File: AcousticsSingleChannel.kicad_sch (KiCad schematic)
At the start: 24 parts, among them J1 SSW-104-01-G-D, J2 TSW-104-07-F-D, U1 OPA1604AIPWR, U2 ADS127L21IRUKT, U4 mcp1416t-e/ot

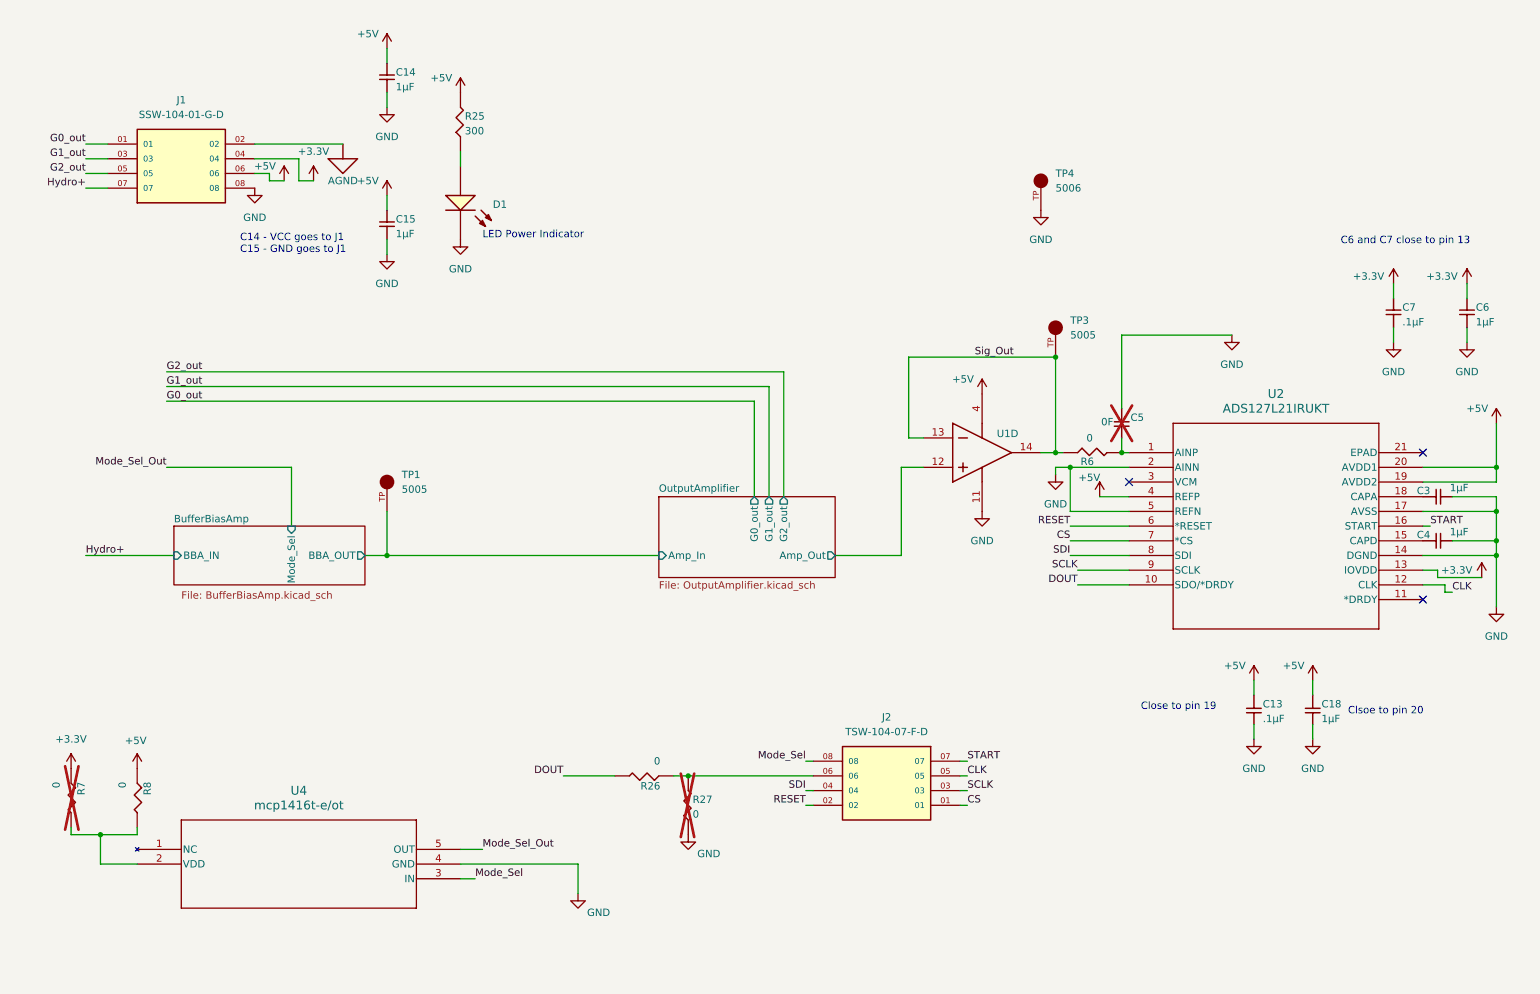
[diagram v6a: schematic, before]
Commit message: Changed headers.
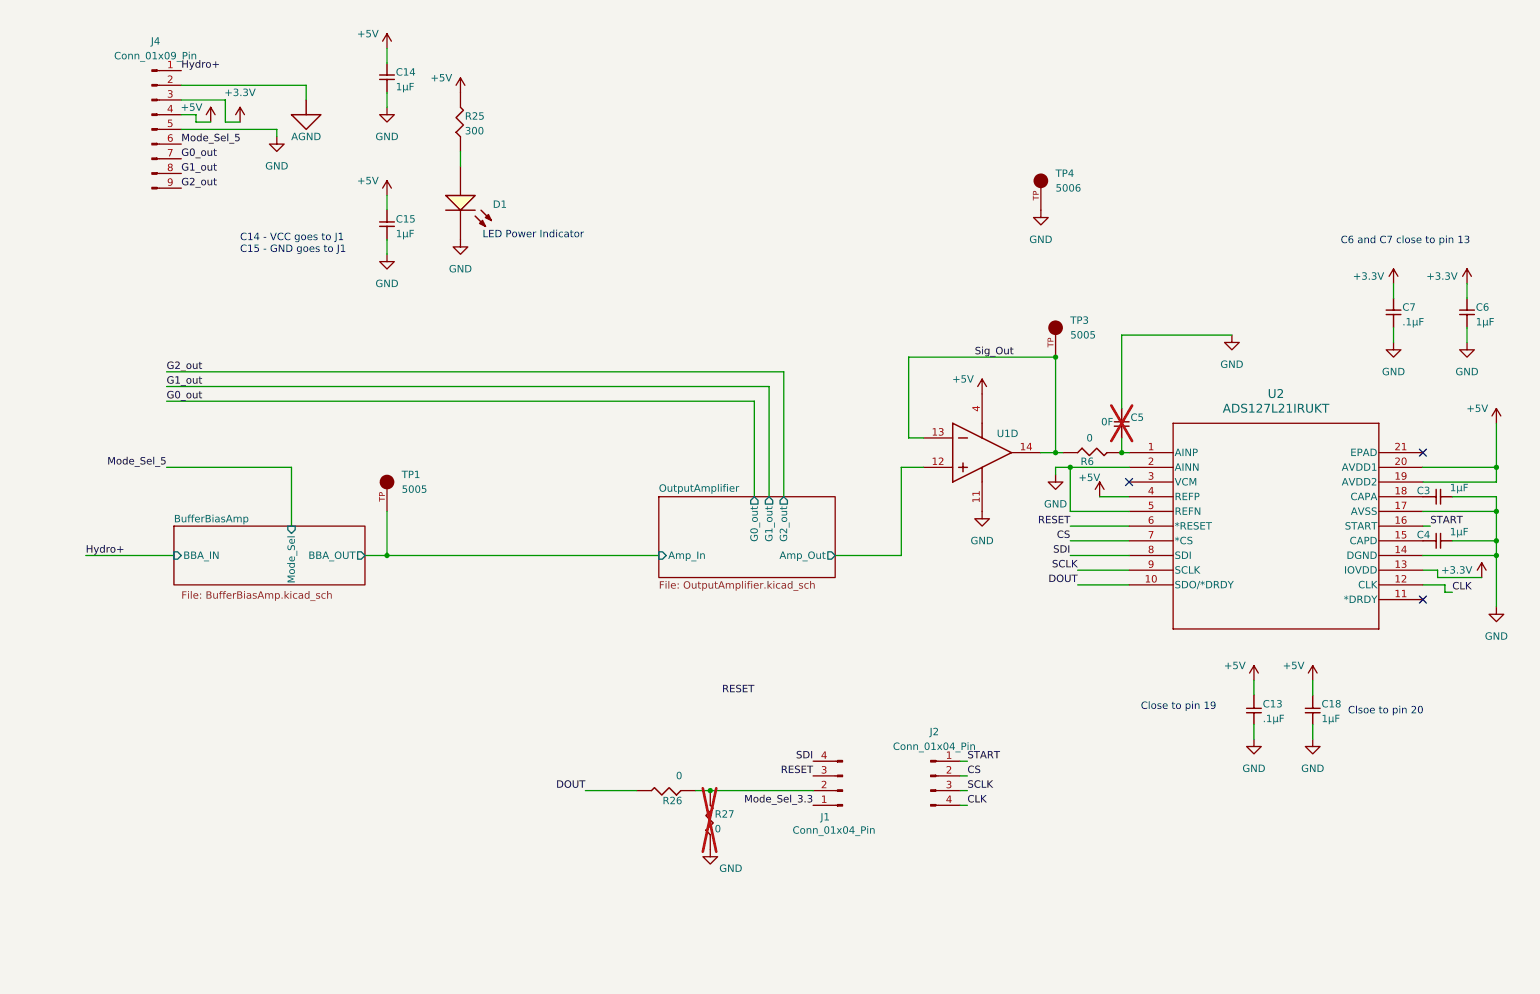
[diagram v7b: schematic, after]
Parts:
- removed J1: SSW-104-01-G-D, Accoustics:SAMTEC_SSW-104-01-G-D, symbol Accoustics:SSW-104-01-G-D
- removed J2: TSW-104-07-F-D, Accoustics:SAMTEC_TSW-104-07-F-D, symbol Accoustics:TSW-104-07-F-D
- removed R7, R8: 0, AltiumImports:SMD-0603-RES, symbol AcousticsSingleChannel-altium-import:root_0_ERJ-3EKF7500V
- removed U4: mcp1416t-e/ot, Accoustics:SOT-23-5_MC_MCH-M, symbol Accoustics:mcp1416t-e_ot
- added J1, J2: Conn_01x04_Pin, Connector_PinHeader_2.54mm:PinHeader_1x04_P2.54mm_Vertical, symbol Connector:Conn_01x04_Pin
- added J4: Conn_01x09_Pin, Connector_PinHeader_2.54mm:PinHeader_1x09_P2.54mm_Vertical, symbol Connector:Conn_01x09_Pin
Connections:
- net +3.3V: now also J4.3 (Pin_3)
- net +5V: now also J4.4 (Pin_4)
- net AGND: now also J4.2 (Pin_2)
- net CLK: now also J2.4 (Pin_4)
- net CS: now also J2.2 (Pin_2)
- net G0_out: now also J4.7 (Pin_7)
- net G1_out: now also J4.8 (Pin_8)
- net G2_out: now also J4.9 (Pin_9)
- net GND: now also J4.5 (Pin_5)
- net Hydro+: now also J4.1 (Pin_1)
- net RESET: now also J1.3 (Pin_3)
- net SCLK: now also J2.3 (Pin_3)
- net SDI: now also J1.4 (Pin_4)
- net START: now also J2.1 (Pin_1)
- net at R26.1, R27.2: now also J1.2 (Pin_2)
- new net Mode_Sel_3.3: J1.1 (Pin_1)
- new net Mode_Sel_5: J4.6 (Pin_6)
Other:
- moved on the sheet: R26, R27

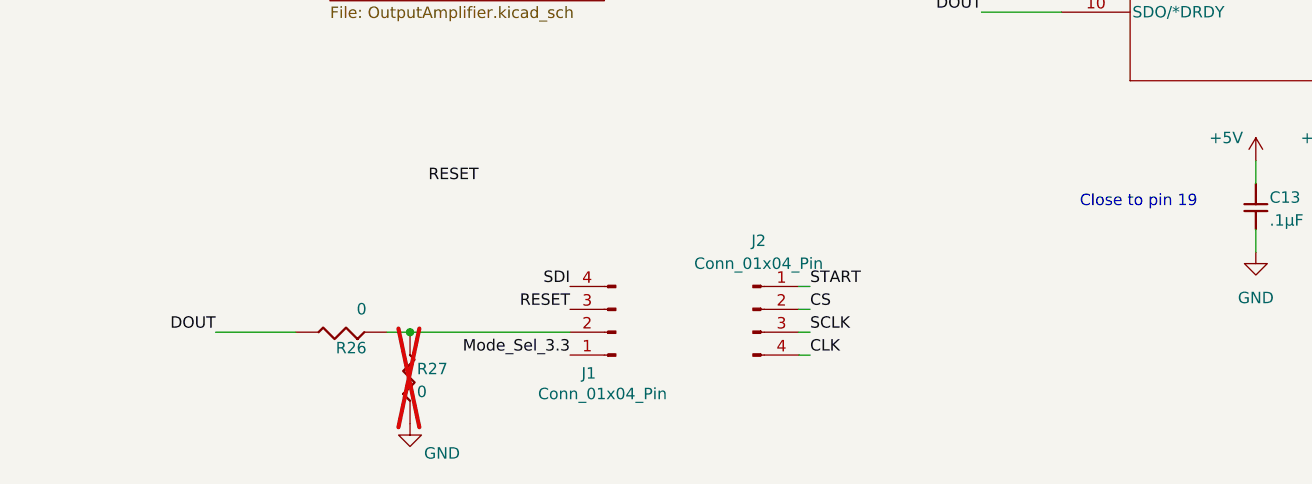
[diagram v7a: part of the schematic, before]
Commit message: changed pinouts, causing major changes to layout mostly on layer1.
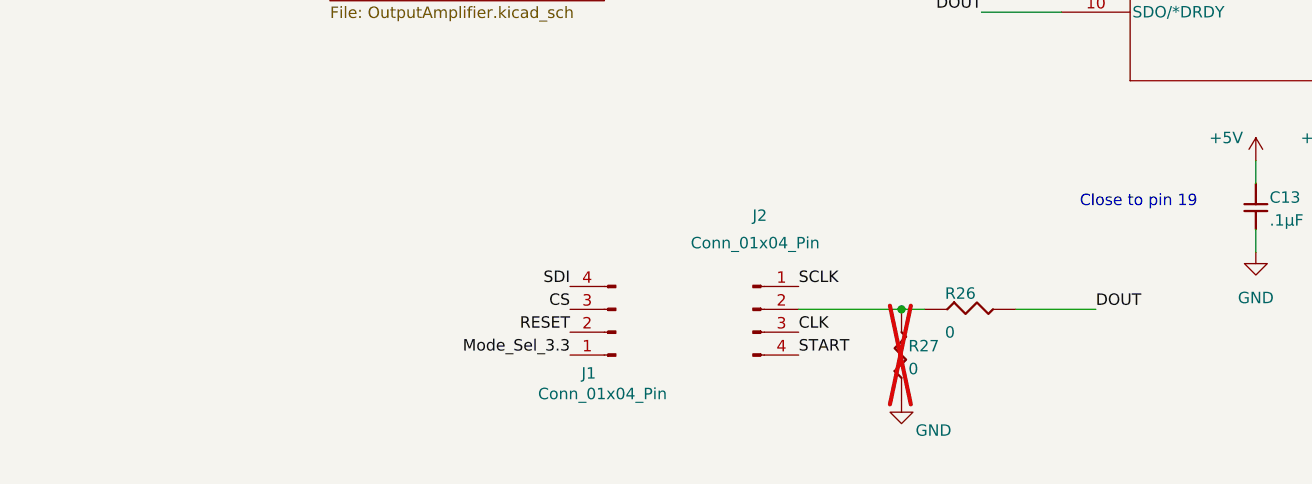
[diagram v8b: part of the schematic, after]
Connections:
- net CLK: now also J2.3 (Pin_3); no longer J2.4 (Pin_4)
- net CS: now also J1.3 (Pin_3); no longer J2.2 (Pin_2)
- net RESET: now also J1.2 (Pin_2); no longer J1.3 (Pin_3)
- net SCLK: now also J2.1 (Pin_1); no longer J2.3 (Pin_3)
- net START: now also J2.4 (Pin_4); no longer J2.1 (Pin_1)
- net at R26.1, R27.2: now also J2.2 (Pin_2); no longer J1.2 (Pin_2)
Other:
- moved on the sheet: R26, R27
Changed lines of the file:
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@@
 	)
 	(junction
-		(at 128.27 152.4)
+		(at 182.88 149.86)
 		(diameter 0)
 		(color 0 0 0 0)
@@
 	(wire
 		(pts
-			(xy 115.57 152.4) (xy 106.68 152.4)
+			(xy 195.58 149.86) (xy 204.47 149.86)
 		)
 		(stroke
@@
 	(wire
 		(pts
-			(xy 171.45 154.94) (xy 172.72 154.94)
-		)
-		(stroke
-			(width 0)
-			(type default)
-		)
-	)
-	(wire
-		(pts
-			(xy 172.72 147.32) (xy 171.45 147.32)
-		)
-		(stroke
-			(width 0)
-			(type default)
-		)
-	)
-	(wire
-		(pts
 			(xy 68.58 111.76) (xy 72.39 111.76)
 		)
@@
 	(wire
 		(pts
-			(xy 128.27 152.4) (xy 146.05 152.4)
-		)
-		(stroke
-			(width 0)
-			(type default)
-		)
-	)
-	(wire
-		(pts
 			(xy 53.34 39.37) (xy 53.34 38.1)
 		)
@@
 	(wire
 		(pts
-			(xy 171.45 152.4) (xy 172.72 152.4)
-		)
-		(stroke
-			(width 0)
-			(type default)
-		)
-	)
-	(wire
-		(pts
 			(xy 39.37 36.83) (xy 41.91 36.83)
 		)
@@
 	(wire
 		(pts
-			(xy 125.73 152.4) (xy 128.27 152.4)
+			(xy 185.42 149.86) (xy 182.88 149.86)
 		)
 		(stroke
@@
 	(wire
 		(pts
-			(xy 171.45 149.86) (xy 172.72 149.86)
+			(xy 171.45 149.86) (xy 182.88 149.86)
 		)
 		(stroke
@@
 		)
 	)
-	(label "SDI"
-		(at 146.05 147.32 180)
+	(label "G2_out"
+		(at 36.83 48.26 0)
 		(effects
 			(font
 				(size 1.27 1.27)
 			)
-			(justify right bottom)
+			(justify left bottom)
 		)
 	)
-	(label "G0_out"
-		(at 36.83 43.18 0)
+	(label "G1_out"
+		(at 36.83 45.72 0)
 		(effects
 			(font
@@
 		)
 	)
-	(label "G1_out"
-		(at 36.83 45.72 0)
+	(label "SCLK"
+		(at 171.45 147.32 0)
 		(effects
 			(font
@@
 		)
 	)
+	(label "G0_out"
+		(at 36.83 43.18 0)
+		(effects
+			(font
+				(size 1.27 1.27)
+			)
+			(justify left bottom)
+		)
+	)
 	(label "Mode_Sel_5"
 		(at 36.83 40.64 0)
@@
 		)
 	)
-	(label "CS"
-		(at 172.72 149.86 0)
+	(label "START"
+		(at 171.45 154.94 0)
 		(effects
 			(font
@@
 		)
 	)
-	(label "RESET"
-		(at 146.05 149.86 180)
-		(effects
-			(font
-				(size 1.27 1.27)
-			)
-			(justify right bottom)
-		)
-	)
-	(label "SCLK"
-		(at 172.72 152.4 0)
+	(label "G0_out"
+		(at 34.29 85.09 0)
 		(effects
 			(font
@@
 		)
 	)
-	(label "RESET"
-		(at 135.89 135.89 180)
+	(label "G1_out"
+		(at 34.29 82.55 0)
 		(effects
 			(font
 				(size 1.27 1.27)
 			)
-			(justify right bottom)
+			(justify left bottom)
 		)
 	)
-	(label "G0_out"
-		(at 34.29 85.09 0)
+	(label "G2_out"
+		(at 34.29 80.01 0)
 		(effects
 			(font
@@
 	)
 	(label "CLK"
-		(at 172.72 154.94 0)
+		(at 171.45 152.4 0)
 		(effects
 			(font
@@
 		)
 	)
-	(label "G1_out"
-		(at 34.29 82.55 0)
+	(label "DOUT"
+		(at 204.47 149.86 0)
 		(effects
 			(font
@@
 		)
 	)
-	(label "G2_out"
-		(at 34.29 80.01 0)
+	(label "SDI"
+		(at 190.5 111.76 180)
 		(effects
 			(font
 				(size 1.27 1.27)
 			)
-			(justify left bottom)
+			(justify right bottom)
 		)
 	)
-	(label "DOUT"
-		(at 106.68 152.4 180)
+	(label "SDI"
+		(at 146.05 147.32 180)
 		(effects
 			(font
@@
 		)
 	)
-	(label "G2_out"
-		(at 36.83 48.26 0)
+	(label "Sig_Out"
+		(at 173.99 77.47 0)
 		(effects
 			(font
@@
 		)
 	)
-	(label "SDI"
-		(at 190.5 111.76 180)
+	(label "CS"
+		(at 146.05 149.86 180)
 		(effects
 			(font
@@
 		)
 	)
-	(label "Sig_Out"
-		(at 173.99 77.47 0)
-		(effects
-			(font
-				(size 1.27 1.27)
-			)
-			(justify left bottom)
-		)
-	)
 	(label "DOUT"
 		(at 191.77 116.84 180)
@@
 		)
 	)
-	(label "START"
-		(at 172.72 147.32 0)
+	(label "RESET"
+		(at 146.05 152.4 180)
 		(effects
 			(font
 				(size 1.27 1.27)
 			)
-			(justify left bottom)
+			(justify right bottom)
 		)
 	)
@@
 	(symbol
 		(lib_id "power:GND")
-		(at 128.27 162.56 0)
+		(at 182.88 160.02 0)
 		(unit 1)
 		(exclude_from_sim no)
@@
 		(dnp no)
 		(property "Reference" "#PWR017"
-			(at 128.27 168.91 0)
+			(at 182.88 166.37 0)
 			(effects
 				(font
@@
 		)
 		(property "Value" "GND"
-			(at 131.826 165.862 0)
+			(at 186.436 163.322 0)
 			(effects
 				(font
@@
 		)
 		(property "Footprint" ""
-			(at 128.27 162.56 0)
+			(at 182.88 160.02 0)
 			(effects
 				(font
@@
 		)
 		(property "Datasheet" ""
-			(at 128.27 162.56 0)
+			(at 182.88 160.02 0)
 			(effects
 				(font
@@
 		)
 		(property "Description" "Power symbol creates a global label with name \"GND\" , ground"
-			(at 128.27 162.56 0)
+			(at 182.88 160.02 0)
 			(effects
 				(font
@@
 		(on_board yes)
 		(dnp no)
-		(fields_autoplaced yes)
 		(property "Reference" "J2"
-			(at 167.005 142.24 0)
+			(at 167.132 139.446 0)
 			(effects
 				(font
@@
 		)
 		(property "Value" "Conn_01x04_Pin"
-			(at 167.005 144.78 0)
+			(at 166.624 142.494 0)
 			(effects
 				(font
@@
 	(symbol
 		(lib_id "AcousticsSingleChannel-altium-import:root_0_ERJ-3EKF7500V")
-		(at 120.65 152.4 180)
+		(at 190.5 149.86 0)
 		(unit 1)
 		(exclude_from_sim no)
@@
 		(dnp no)
 		(property "Reference" "R26"
-			(at 123.444 153.416 0)
+			(at 187.706 148.844 0)
 			(effects
 				(font
@@
 		)
 		(property "Value" "0"
-			(at 123.444 149.098 0)
+			(at 187.706 153.162 0)
 			(effects
 				(font
@@
 		)
 		(property "Footprint" "AltiumImports:SMD-0603-RES"
-			(at 120.65 152.4 0)
+			(at 190.5 149.86 0)
 			(effects
 				(font
@@
 		)
 		(property "Datasheet" ""
-			(at 120.65 152.4 0)
+			(at 190.5 149.86 0)
 			(effects
 				(font
@@
 		)
 		(property "Description" ""
-			(at 120.65 152.4 0)
+			(at 190.5 149.86 0)
 			(effects
 				(font
@@
 		)
 		(property "Part Number" "ERJ-3EKF7500V"
-			(at 120.65 152.4 0)
+			(at 190.5 149.86 0)
 			(effects
 				(font
@@
 	(symbol
 		(lib_id "AcousticsSingleChannel-altium-import:root_1_ERJ-3EKF1001V")
-		(at 128.27 157.48 0)
+		(at 182.88 154.94 0)
 		(unit 1)
 		(exclude_from_sim no)
@@
 		(dnp yes)
 		(property "Reference" "R27"
-			(at 129.032 157.226 0)
+			(at 183.642 154.686 0)
 			(effects
 				(font
@@
 		)
 		(property "Value" "0"
-			(at 129.032 159.766 0)
+			(at 183.642 157.226 0)
 			(effects
 				(font
@@
 		)
 		(property "Footprint" "AltiumImports:SMD-0603-RES"
-			(at 128.27 157.48 0)
+			(at 182.88 154.94 0)
 			(effects
 				(font
@@
 		)
 		(property "Datasheet" ""
-			(at 128.27 157.48 0)
+			(at 182.88 154.94 0)
 			(effects
 				(font
@@
 		)
 		(property "Description" ""
-			(at 128.27 157.48 0)
+			(at 182.88 154.94 0)
 			(effects
 				(font
@@
 		)
 		(property "Part Number" "ERJ-3EKF1001V"
-			(at 128.27 157.48 0)
+			(at 182.88 154.94 0)
 			(effects
 				(font
